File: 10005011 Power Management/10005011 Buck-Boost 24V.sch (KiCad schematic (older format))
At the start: 63 parts, among them IC10 LTC3780, IC9 LT1620CMS8, T19 SI7884BDP, T20 SI7884BDP, T21 SI7884BDP, T22 SI7884BDP

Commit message: extracted footprints of sheet7, and association in sch
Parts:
- C115, C116, C117, C118, C119, C37, C49, C52: footprint 10106052 PowerPack:CAPC1608X86N -> 10005011 Power Management:C0603_1
- C125: footprint (none) -> 10005011 Power Management:C-SC10_1; symbol Device:CP -> 10005011_Power_Management:CP
- C131, C30, C31, C32: footprint (none) -> 10005011 Power Management:C0805_1
- C134, C135, C29: footprint (none) -> 10005011 Power Management:C1210_1
- C136, C137, C138, C26, C27, C28, C40, C41, C43: footprint (none) -> 10005011 Power Management:C2220_1
- C25, C48: footprint (none) -> 10005011 Power Management:C0402_1
- C33, C50, R62: footprint (none) -> 10005011 Power Management:RC1206_1
- C38, C39, C56: footprint (none) -> 10005011 Power Management:C0603_1
- C42: symbol Device:CP -> 10005011_Power_Management:CP
- CR2: footprint Diode_SMD:D_SOD-123 -> 10005011 Power Management:SOD123-AK_1; symbol 10005011_Power_Management_Schematic_Symbols:1N5819 -> 10005011_Power_Management:1N5819
- D12: footprint Diode_SMD:D_SOT-23_ANK -> 10005011 Power Management:SOT23-1DIODE_1
- D5, D6: footprint Diode_SMD:D_SMB -> 10005011 Power Management:SMB_1
- FLTR1, FLTR2: footprint 10106052 PowerPack:BNX00201 -> 10005011 Power Management:BNX002+SF-AIROX_1
- IC10: footprint (none) -> 10005011 Power Management:SSOP24_1
- IC9: footprint (none) -> 10005011 Power Management:uSO08_1
- L3: footprint (none) -> 10005011 Power Management:SF-3863-WESI_1
- R117: footprint (none) -> 10005011 Power Management:R0805_1
- R58, R60, R64, R65, R66, R74: footprint (none) -> 10005011 Power Management:R0603_1
- R75: footprint (none) -> 10005011 Power Management:R2512_1
- R76: renamed from R?; footprint (none) -> 10005011 Power Management:R0603_1
- T19, T20, T21, T22: footprint Package_SO:PowerPAK_SO-8_Single -> 10005011 Power Management:SO08-PPAD_SI7884_1
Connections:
- net GND: now also C25.2; no longer C25.1, IC9.7 (PROG)
- net INTVCC-1: now also CR2.A, R60.2; no longer CR2.2 (A), R60.1
- net PGND: now also C115.1, C116.1, C117.1, C118.1, C119.1, C125.-, C134.1, C135.1, C26.1, C27.1, C28.1, C29.1, C31.1, C42.-, R76.1; no longer C115.2, C116.2, C117.2, C118.2, C119.2, C125.2, C134.2, C135.2, C26.2, C27.2, C28.2, C29.2, C31.2, C42.2, R76.2
- net SW1: now also C38.1; no longer C38.2
- net SW2: now also C39.1; no longer C39.2
- net VALIM: now also C116.2, C118.2; no longer C116.1, C118.1
- net VIN: now also C115.2, C125.+, C134.2, C135.2, C26.2, C27.2, C28.2, C29.2, C31.2; no longer C115.1, C125.1, C134.1, C135.1, C26.1, C27.1, C28.1, C29.1, C31.1
- net VOSENSE-1: now also R63.1; no longer R63.2
- net at FLTR2.CB, IC9.4 (IN-), R62.1: now also C117.2, C37.2, R63.2; no longer C117.1, C37.1, R63.1
- net at D6.A, R75.2, T21.S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: now also R74.1; no longer R74.2
- net at C136.1, C137.1, C138.1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: now also C37.1, C42.+; no longer C37.2, C42.1
- net at C56.2, IC10.3 (SENSE+): now also R74.2; no longer R74.1
- net at C56.1, IC10.4 (SENSE-): now also R76.2; no longer R76.1
- net at IC10.1 (PGOOD): now also R60.1; no longer R60.2
- net at CR1.1 (K), IC10.24 (BOOST1): now also C38.2; no longer C38.1
- net at D12.K, IC9.6 (VCC), R117.1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: now also C25.1, C33.2; no longer C25.2
- net at IC9.8 (AVG): now also C33.1; no longer C33.2
- net at R59.1, R61.2: now also IC9.7 (PROG); no longer C33.1
- net at R64.1, R66.1: now also C119.2; no longer C119.1
- new net: C39.2, CR2.K, IC10.13 (BOOST2)
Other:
- moved on the sheet: C116, R59, R61

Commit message: footprints and sch sheet6 association and orientation
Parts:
- C25: Manufacturer (none) -> MURATA; Manufacturer_No (none) -> GRM155R71C104JA88J
- C42: footprint (none) -> 10005011 Power Management:C-SC10_1
- D5, D6: symbol 10005011_Power_Management_Schematic_Symbols:STPS340U -> 10005011_Power_Management:STPS340U
- FLTR1, FLTR2: Description (none) -> FILTER CC, 1MHZ-1GHZ, 10A, 50V
- R59, R61, R63, R67: footprint (none) -> 10005011 Power Management:R0603_1
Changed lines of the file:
@@
 F 6 "BNX002-11" H 1750 1400 50  0001 C CNN "MPN"
 F 7 "BNX002-11" H 1750 1400 50  0001 C CNN "Manufacturer_No"
+F 8 "FILTER CC, 1MHZ-1GHZ, 10A, 50V" H 1750 1400 50  0001 C CNN "Description"
 	1    1750 1400
 	1    0    0    -1
@@
 F 6 "BNX002-11" H 14200 1350 50  0001 C CNN "MPN"
 F 7 "BNX002-11" H 14200 1350 50  0001 C CNN "Manufacturer_No"
+F 8 "FILTER CC, 1MHZ-1GHZ, 10A, 50V" H 14200 1350 50  0001 C CNN "Description"
 	1    14200 1350
 	-1   0    0    -1
@@
 F 0 "C42" H 10700 1850 50  0000 C CNN
 F 1 "330uF" H 10700 1750 50  0000 C CNN
-F 2 "" H 10738 1300 50  0001 C CNN
+F 2 "10005011 Power Management:C-SC10_1" H 10738 1300 50  0001 C CNN
 F 3 "" H 10700 1450 50  0001 C CNN
 F 4 "CAPACITOR ELECTROLYTIC, 330UF,35V" H 10700 1450 50  0001 C CNN "Description"
@@
 F 0 "R63" H 12831 2104 50  0000 R CNN
 F 1 "47k" H 12831 2195 50  0000 R CNN
-F 2 "" V 12830 2150 50  0001 C CNN
+F 2 "10005011 Power Management:R0603_1" V 12830 2150 50  0001 C CNN
 F 3 "" H 12900 2150 50  0001 C CNN
 F 4 "RESISTOR,47K OHM,0.063W,+/-0.1%,0603" H 12900 2150 50  0001 C CNN "Description"
@@
 F 0 "R67" H 12970 2596 50  0000 L CNN
 F 1 "1.62k" H 12970 2505 50  0000 L CNN
-F 2 "" V 12830 2550 50  0001 C CNN
+F 2 "10005011 Power Management:R0603_1" V 12830 2550 50  0001 C CNN
 F 3 "" H 12900 2550 50  0001 C CNN
 F 4 "RESISTOR,1.62K OHM,0.063W,+/0.1%,0603" H 12900 2550 50  0001 C CNN "Description"
@@
 $EndComp
 $Comp
-L 10005011_Power_Management_Schematic_Symbols:STPS340U D5
+L 10005011_Power_Management:STPS340U D5
 U 1 1 5EA7436E
 P 7550 2300
@@
 $EndComp
 $Comp
-L 10005011_Power_Management_Schematic_Symbols:STPS340U D6
+L 10005011_Power_Management:STPS340U D6
 U 1 1 5EA7808F
 P 6650 3200
@@
 F 4 "CAPACITOR,100NF,16V,+/-10%,X7R,0402" H 11100 3850 50  0001 C CNN "Description"
 F 5 "10022607" H 11100 3850 50  0001 C CNN "Item Number"
-F 6 "" H 11100 3850 50  0001 C CNN "Manufacturer"
-F 7 "" H 11100 3850 50  0001 C CNN "Manufacturer_No"
+F 6 "MURATA" H 11100 3850 50  0001 C CNN "Manufacturer"
+F 7 "GRM155R71C104JA88J" H 11100 3850 50  0001 C CNN "Manufacturer_No"
 	1    11100 3850
 	0    -1   -1   0
@@
 F 0 "R61" H 12320 2646 50  0000 L CNN
 F 1 "39k" H 12320 2555 50  0000 L CNN
-F 2 "" V 12180 2600 50  0001 C CNN
+F 2 "10005011 Power Management:R0603_1" V 12180 2600 50  0001 C CNN
 F 3 "" H 12250 2600 50  0001 C CNN
 F 4 "RESISTOR,39K OHM,0.063W,+/-1%,0603" H 12250 2600 50  0001 C CNN "Description"
@@
 F 0 "R59" H 12320 3046 50  0000 L CNN
 F 1 "5.6k" H 12320 2955 50  0000 L CNN
-F 2 "" V 12180 3000 50  0001 C CNN
+F 2 "10005011 Power Management:R0603_1" V 12180 3000 50  0001 C CNN
 F 3 "" H 12250 3000 50  0001 C CNN
 F 4 "RESISTOR,5.6K OHM,0.063W,+/-1%,0603" H 12250 3000 50  0001 C CNN "Description"

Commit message: sheet5 refdes readable position
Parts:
- FLTR1, FLTR2: symbol 10005011_Power_Management:BNX002-11 -> 10005011_Power_Management:BNX002-01
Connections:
- net PGND: now also FLTR1.1, FLTR2.1
- net VALIM: now also FLTR1.4, FLTR2.4
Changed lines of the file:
@@
 $EndComp
 $Comp
-L 10005011_Power_Management:BNX002-11 FLTR1
+L 10005011_Power_Management:BNX002-01 FLTR1
 U 1 1 5E92D027
 P 1750 1400
@@
 $EndComp
 $Comp
-L 10005011_Power_Management:BNX002-11 FLTR2
+L 10005011_Power_Management:BNX002-01 FLTR2
 U 1 1 5E983555
 P 14200 1350

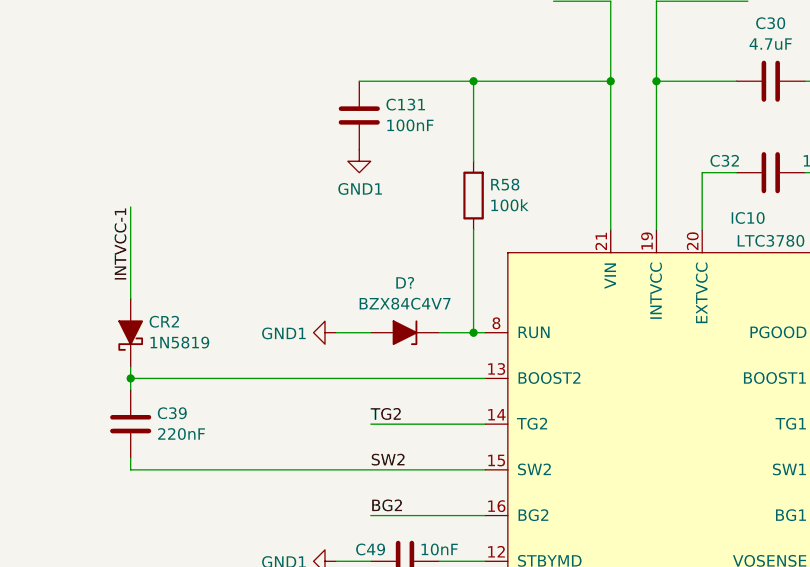
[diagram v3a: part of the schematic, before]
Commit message: all components with refdes
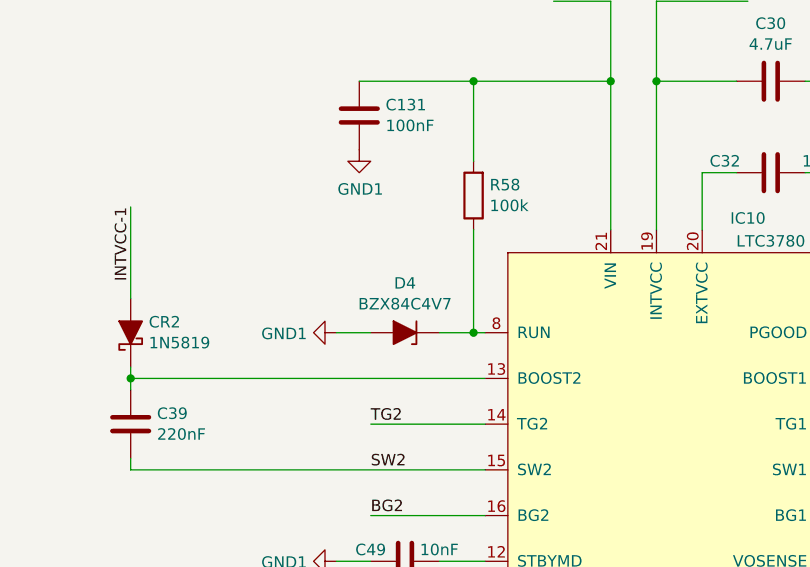
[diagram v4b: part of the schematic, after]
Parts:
- gave numbers to parts that had none: 1
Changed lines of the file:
@@
 $EndComp
 $Comp
-L 10005011_Power_Management_Schematic_Symbols:BZX84C4V7 D?
+L 10005011_Power_Management_Schematic_Symbols:BZX84C4V7 D4
 U 1 1 5ED2FC67
 P 2400 6600
-F 0 "D?" H 2400 6384 50  0000 C CNN
+F 0 "D4" H 2400 6384 50  0000 C CNN
 F 1 "BZX84C4V7" H 2400 6475 50  0000 C CNN
 F 2 "Diode_SMD:D_SOT-23_ANK" H 2400 6600 50  0001 C CNN

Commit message: footprints sheet6 and small fix to sheet7
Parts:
- D4: symbol 10005011_Power_Management_Schematic_Symbols:BZX84C4V7 -> 10005011_Power_Management:BZX84C4V7
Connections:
- net GND: now also D4.A; no longer D4.2 (A)
- net at IC10.8 (RUN), R58.1: now also D4.K; no longer D4.1 (K)
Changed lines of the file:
@@
 $EndComp
 $Comp
-L 10005011_Power_Management_Schematic_Symbols:BZX84C4V7 D4
+L 10005011_Power_Management:BZX84C4V7 D4
 U 1 1 5ED2FC67
 P 2400 6600

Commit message: assigned footprints with cmp file
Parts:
- CR1: footprint Diode_SMD:D_SOD-123 -> 10005011 Power Management:SOD123-AK_1
- D4: footprint Diode_SMD:D_SOT-23_ANK -> 10005011 Power Management:SOT23-1DIODE_1
- FLTR2: footprint 10005011 Power Management:BNX002+SF-AIROX_1 -> 10005011 Power Management:BNX002_1
- JPL1: footprint (none) -> 10005011 Power Management:GDCAFE-F_FERME_1
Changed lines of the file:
@@
 F 0 "FLTR2" H 14175 1845 50  0000 C CNN
 F 1 "BNX002-11" H 14175 1754 50  0000 C CNN
-F 2 "10005011 Power Management:BNX002+SF-AIROX_1" H 14090 1370 50  0001 C CNN
+F 2 "10005011 Power Management:BNX002_1" H 14090 1370 50  0001 C CNN
 F 3 "https://www.murata.com/en-us/api/pdfdownloadapi?cate=luNoiseSupprFilteBlockType&partno=BNX002-11" H 14090 1370 50  0001 C CNN
 F 4 "10022532" H 14090 1370 50  0001 C CNN "Item Number"
@@
 F 0 "JPL1" H 2950 9381 50  0000 C CNN
 F 1 "GROUND_LINK" H 2950 9290 50  0000 C CNN
-F 2 "" H 2950 9200 50  0001 C CNN
+F 2 "10005011 Power Management:GDCAFE-F_FERME_1" H 2950 9200 50  0001 C CNN
 F 3 "~" H 2950 9200 50  0001 C CNN
 	1    2950 9200
@@
 F 0 "CR1" V 5246 6521 50  0000 R CNN
 F 1 "1N5819" V 5155 6521 50  0000 R CNN
-F 2 "Diode_SMD:D_SOD-123" H 5200 6600 50  0001 C CNN
+F 2 "10005011 Power Management:SOD123-AK_1" H 5200 6600 50  0001 C CNN
 F 3 "https://www.diodes.com/assets/Datasheets/ds30217.pdf" H 5200 6600 50  0001 C CNN
 F 4 "Diodes Incorporated" H 5200 6600 50  0001 C CNN "Mfgr"
@@
 F 0 "D4" H 2400 6384 50  0000 C CNN
 F 1 "BZX84C4V7" H 2400 6475 50  0000 C CNN
-F 2 "Diode_SMD:D_SOT-23_ANK" H 2400 6600 50  0001 C CNN
+F 2 "10005011 Power Management:SOT23-1DIODE_1" H 2400 6600 50  0001 C CNN
 F 3 "https://4donline.ihs.com/images/VipMasterIC/IC/ONSM/ONSM-S-A0003405162/ONSM-S-A0003405162-1.pdf?hkey=EC6BD57738AE6E33B588C5F9AD3CEFA7" H 2400 6600 50  0001 C CNN
 F 4 "Rochester Electronics, LLC" H 2400 6600 50  0001 C CNN "Mfgr"

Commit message: conflict solved, two FLTR2
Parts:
- FLTR3: renamed from FLTR2; footprint 10005011 Power Management:BNX002_1 -> 10005011 Power Management:BNX002+SF-AIROX_1
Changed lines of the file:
@@
-$EndComp
-$Comp
-L 10005011_Power_Management:BNX002-01 FLTR2
-U 1 1 5E983555
-P 14200 1350
-F 0 "FLTR2" H 14175 1845 50  0000 C CNN
-F 1 "BNX002-11" H 14175 1754 50  0000 C CNN
-F 2 "10005011 Power Management:BNX002_1" H 14090 1370 50  0001 C CNN
-F 3 "https://www.murata.com/en-us/api/pdfdownloadapi?cate=luNoiseSupprFilteBlockType&partno=BNX002-11" H 14090 1370 50  0001 C CNN
-F 4 "10022532" H 14090 1370 50  0001 C CNN "Item Number"
-F 5 "Murata" H 14090 1370 50  0001 C CNN "Manufacturer"
-F 6 "BNX002-11" H 14200 1350 50  0001 C CNN "MPN"
-F 7 "BNX002-11" H 14200 1350 50  0001 C CNN "Manufacturer_No"
-F 8 "FILTER CC, 1MHZ-1GHZ, 10A, 50V" H 14200 1350 50  0001 C CNN "Description"
-	1    14200 1350
-	-1   0    0    -1
 $EndComp
 $Comp
@@
 Wire Wire Line
 	14800 1250 14650 1250
+$Comp
+L 10005011_Power_Management:BNX002-01 FLTR3
+U 1 1 5E983555
+P 14200 1350
+F 0 "FLTR3" H 14175 1845 50  0000 C CNN
+F 1 "BNX002-11" H 14175 1754 50  0000 C CNN
+F 2 "10005011 Power Management:BNX002+SF-AIROX_1" H 14090 1370 50  0001 C CNN
+F 3 "https://www.murata.com/en-us/api/pdfdownloadapi?cate=luNoiseSupprFilteBlockType&partno=BNX002-11" H 14090 1370 50  0001 C CNN
+F 4 "10022532" H 14090 1370 50  0001 C CNN "Item Number"
+F 5 "Murata" H 14090 1370 50  0001 C CNN "Manufacturer"
+F 6 "BNX002-11" H 14200 1350 50  0001 C CNN "MPN"
+F 7 "BNX002-11" H 14200 1350 50  0001 C CNN "Manufacturer_No"
+F 8 "FILTER CC, 1MHZ-1GHZ, 10A, 50V" H 14200 1350 50  0001 C CNN "Description"
+	1    14200 1350
+	-1   0    0    -1
+$EndComp
 $EndSCHEMATC

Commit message: Powermanagement dev netlist fix
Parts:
- CR1: symbol 10005011_Power_Management_Schematic_Symbols:1N5819 -> 10005011_Power_Management:1N5819
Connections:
- net INTVCC-1: now also CR1.A; no longer CR1.2 (A)
- net at C38.2, IC10.24 (BOOST1): now also CR1.K; no longer CR1.1 (K)
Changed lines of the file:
@@
 $EndComp
 $Comp
-L 10005011_Power_Management_Schematic_Symbols:1N5819 CR1
+L 10005011_Power_Management:1N5819 CR1
 U 1 1 5ED2EC1E
 P 5200 6600
